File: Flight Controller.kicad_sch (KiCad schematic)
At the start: 92 parts, among them IC1 ICM-20689, IC2 AT7456E, J1 Micro_SD_Card, P1 USB_C_Plug_USB2.0, Q1 BC817W, SW2 SW_SPDT_321, U1 NCP1117-3.3_SOT223, U1 STM32F405RGTx, U2 LM2575-5.0BU, U3 BMP280, Y1 Resonator

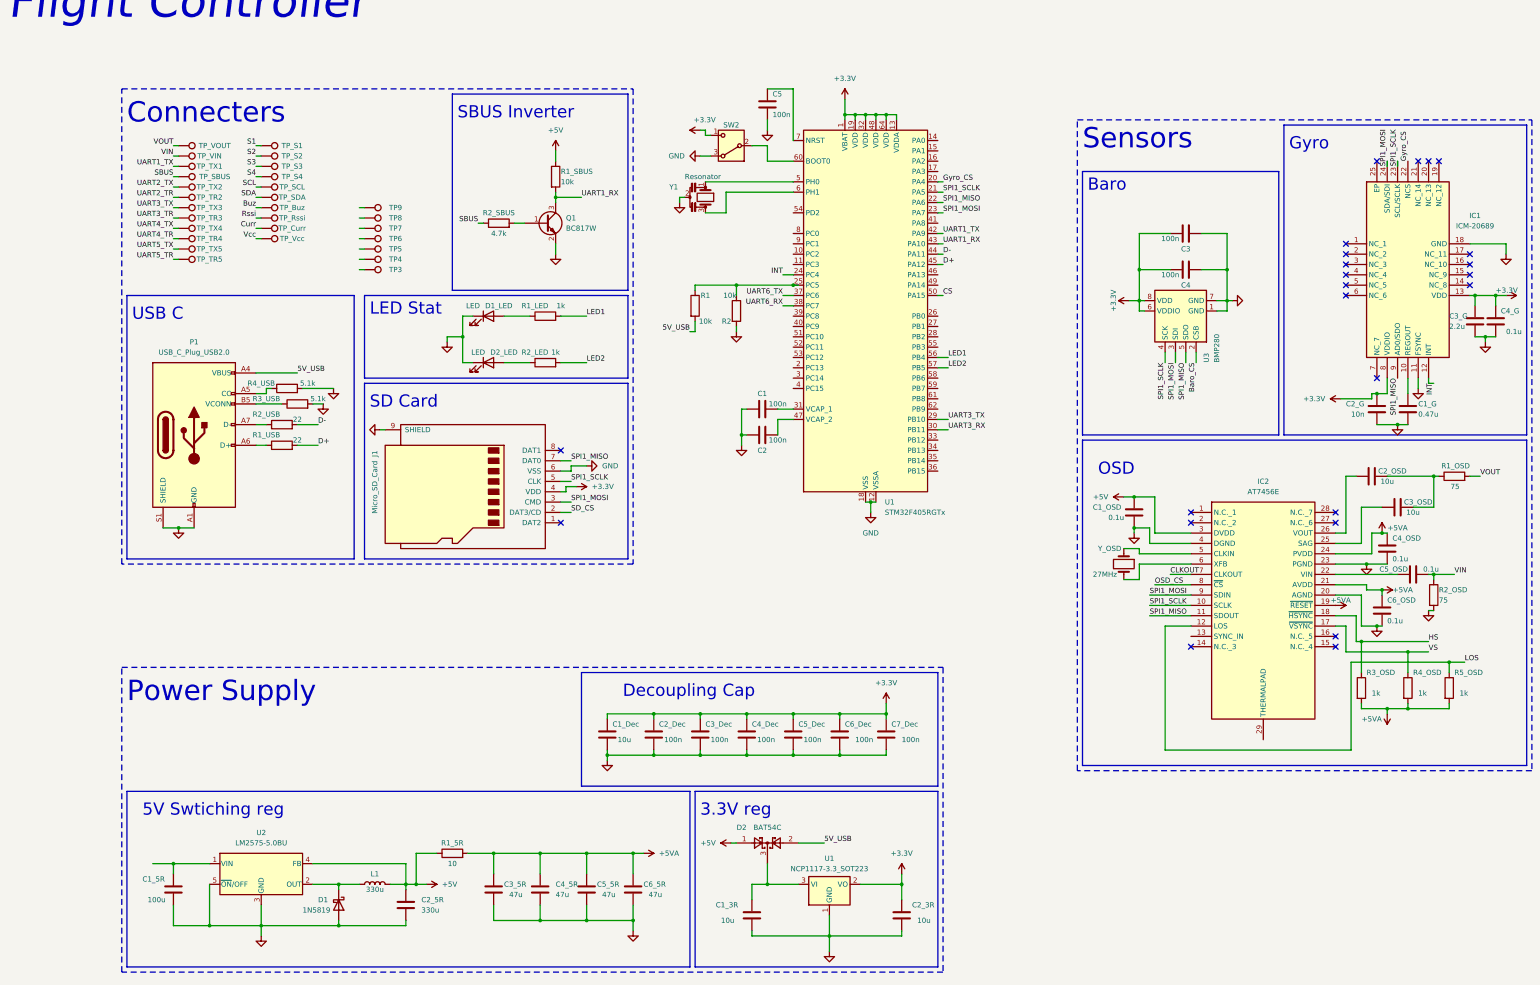
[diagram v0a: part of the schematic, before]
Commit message: schematic update
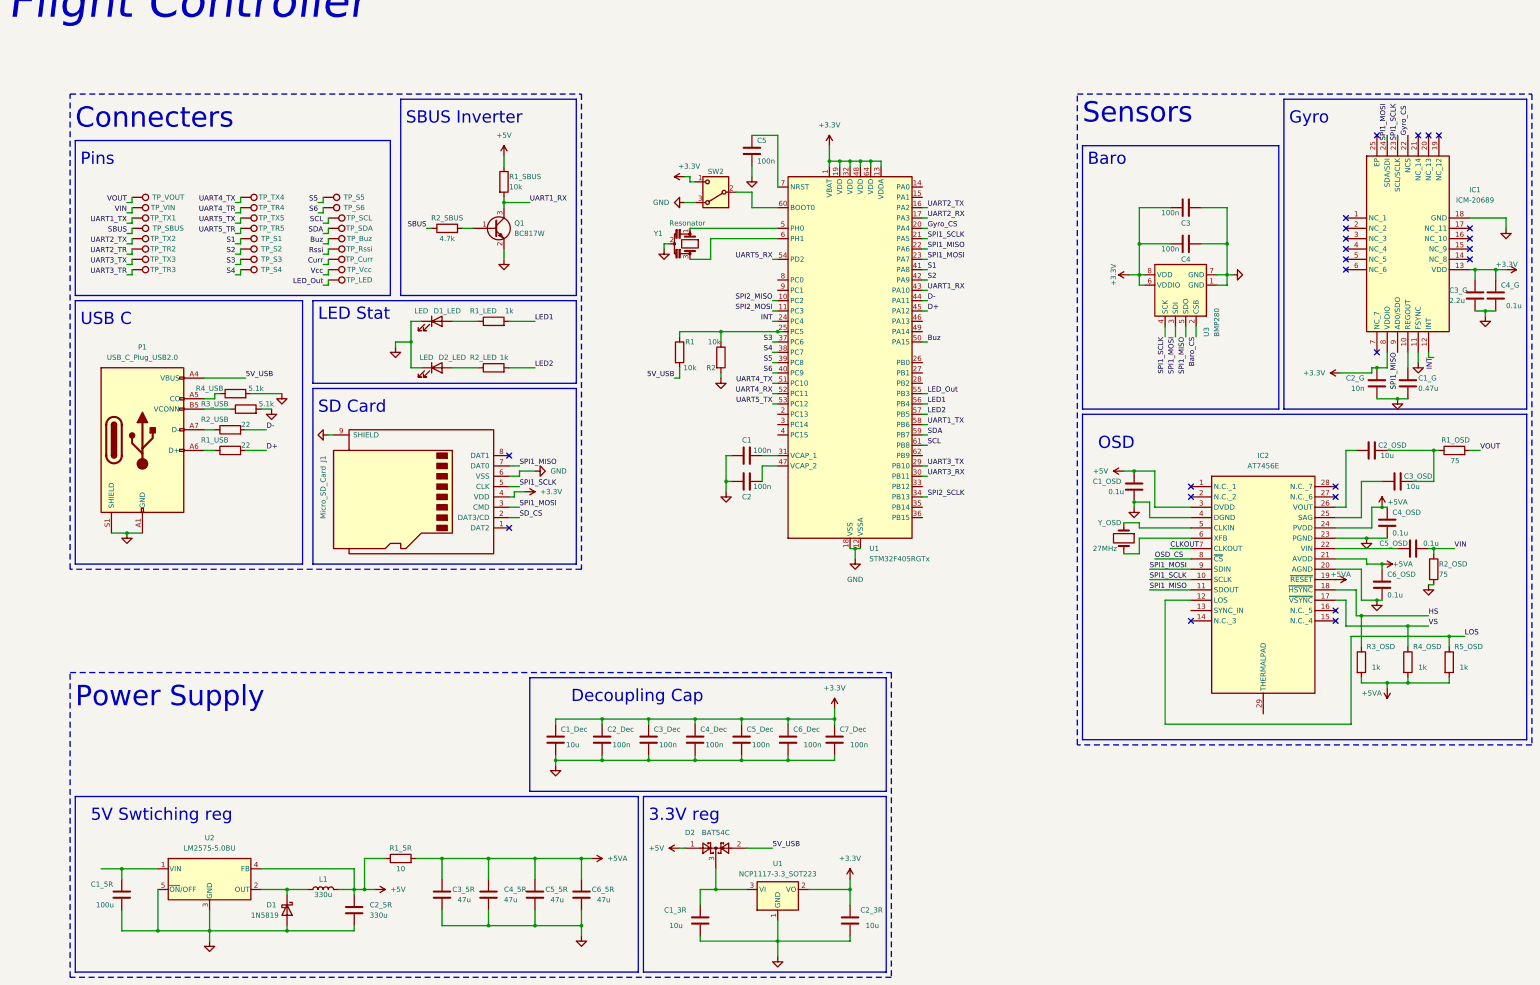
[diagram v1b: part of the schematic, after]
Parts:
- removed TP3, TP4, TP6, TP7: TestPoint, TestPoint:TestPoint_Pad_D2.5mm, symbol Connector:TestPoint
- renumbered TP5 to TP_LED, TP9 to TP_S5, TP8 to TP_S6
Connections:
- net CS is gone; now on net Buz: U1.50 (PA15)
- net UART6_RX is gone; now on net S4: U1.38 (PC7)
- net UART6_TX is gone; now on net S3: U1.37 (PC6)
- net S1: now also U1.41 (PA8)
- net S2: now also U1.42 (PA9)
- net SCL: now also U1.61 (PB8)
- net SDA: now also U1.59 (PB7)
- net UART1_TX: now also U1.58 (PB6); no longer U1.42 (PA9)
- net UART2_TX: now also U1.16 (PA2)
- net UART4_TX: now also U1.51 (PC10)
- net UART5_TX: now also U1.53 (PC12)
- net LED_Out: now reaches TP_LED.1
- net LED_Out: now also U1.55 (PB3)
- net S6: now reaches TP_S6.1
- net S6: now also U1.40 (PC9)
- net SPI2_MISO: now reaches U1.10 (PC2)
- net SPI2_MOSI: now reaches U1.11 (PC3)
- net UART2_RX: now reaches U1.17 (PA3)
- net SPI2_SCLK: now reaches U1.34 (PB13)
- net S5: now reaches U1.39 (PC8)
- net S5: now also TP_S5.1
- net UART4_RX: now reaches U1.52 (PC11)
- net UART5_RX: now reaches U1.54 (PD2)
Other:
- note added: "Pins"
- moved on the sheet: C1, C1_3R, C1_5R, C1_Dec, C1_G, C1_OSD, C2, C2_3R, C2_5R, C2_Dec, C2_G, C2_OSD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

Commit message: Update Schematic
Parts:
- removed C3_5R, C4_5R, C5_5R, C6_5R: 47u, symbol Device:C
- removed R1_5R: 10, symbol Device:R
- added H1, H2, H3, H4: MountingHole_Pad, symbol Mechanical:MountingHole_Pad
- added R3_I2C1, R3_I2C2: 5.1k, symbol Device:R
- added SW1: SW_Push, symbol Switch:SW_Push
- added TP_3V1, TP_3V2, TP_5V1, TP_5V10, TP_5V11, TP_5V12, TP_5V2, TP_5V3, TP_5V4, TP_5V5, TP_5V6, TP_5V7, TP_5V8, TP_5V9, TP_GND1, TP_GND10, TP_GND11, TP_GND12, TP_GND13, TP_GND14, TP_GND2, TP_GND3, TP_GND4, TP_GND5, TP_GND6, TP_GND7, TP_GND8, TP_GND9: TestPoint, TestPoint:TestPoint_Pad_D2.5mm, symbol Connector:TestPoint
- renumbered TP_VIN to TP_CAM, TP_TR2 to TP_RX2, TP_TR3 to TP_RX3, TP_TR4 to TP_RX4, TP_TR5 to TP_RX5, TP_Vcc to TP_VBAT, TP_VOUT to TP_VTX
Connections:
- net UART2_TR is gone; now on net UART2_RX: TP_RX2.1
- net UART3_TR is gone; now on net UART3_RX: TP_RX3.1
- net UART4_TR is gone; now on net UART4_RX: TP_RX4.1
- net UART5_TR is gone; now on net UART5_RX: TP_RX5.1
- net +3.3V: now also R3_I2C1.1, R3_I2C2.2, TP_3V1.1, TP_3V2.1
- net +5V: now also TP_5V1.1, TP_5V10.1, TP_5V11.1, TP_5V12.1, TP_5V2.1, TP_5V3.1, TP_5V4.1, TP_5V5.1, TP_5V6.1, TP_5V7.1, TP_5V8.1, TP_5V9.1
- net Curr: now also U1.14 (PA0)
- net GND: now also H1.1, H2.1, H3.1, H4.1, SW1.2, TP_GND1.1, TP_GND10.1, TP_GND11.1, TP_GND12.1, TP_GND13.1, TP_GND14.1, TP_GND2.1, TP_GND3.1, TP_GND4.1, TP_GND5.1, TP_GND6.1, TP_GND7.1, TP_GND8.1, TP_GND9.1
- net Gyro_CS: no longer U1.20 (PA4)
- net Rssi: now also U1.15 (PA1)
- net SBUS: now also TP_TX1.1; no longer TP_SBUS.1
- net SPI1_MISO: no longer IC2.11 (SDOUT)
- net SPI1_MOSI: no longer IC2.9 (SDIN)
- net SPI1_SCLK: no longer IC2.10 (SCLK)
- net SPI2_MISO: now also IC2.11 (SDOUT)
- net SPI2_MOSI: now also IC2.9 (SDIN)
- net SPI2_SCLK: now also IC2.10 (SCLK)
- net UART1_RX: now also TP_SBUS.1; no longer Q1.3 (C), R1_SBUS.2
- net UART1_TX: now also Q1.3 (C), R1_SBUS.2; no longer TP_TX1.1
- net at C5.1, U1.7 (NRST): now also SW1.1
- net SCL renamed I2C_SCL
- net I2C_SCL: now also R3_I2C2.1
- net SDA renamed I2C_SDA
- net I2C_SDA: now also R3_I2C1.2
- net Vcc renamed VBAT
- net VBAT: now also U1.20 (PA4)
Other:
- note added: "Buzzer"
- note added: "Camera"
- note added: "Currents"
- note added: "I2C"
- note added: "LED"
- note added: "Mounting Holes"
- note added: "Power"
- note added: "Signal"
- note added: "UARTS"
- note added: "VTX"
- note removed: "Pins"
- moved on the sheet: C1, C1_3R, C1_5R, C1_Dec, C1_G, C1_OSD, C2, C2_3R, C2_5R, C2_Dec, C2_G, C2_OSD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

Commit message: Update Schematic
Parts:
- added TP_VBAT+, TP_VBAT-: TestPoint, TestPoint:TestPoint_Pad_D2.5mm, symbol Connector:TestPoint
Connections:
- net Baro_CS: now also U1.8 (PC0)
- net GND: now also TP_VBAT-.1
- net Gyro_CS: now also U1.9 (PC1)
- net OSD_CS: now also U1.26 (PB0)
- net SD_CS: now also U1.27 (PB1)
- net SPI1_MISO: no longer J1.7 (DAT0)
- net SPI1_MOSI: no longer J1.3 (CMD)
- net SPI1_SCLK: no longer J1.5 (CLK)
- net SPI2_MISO: now also J1.7 (DAT0)
- net SPI2_MOSI: now also J1.3 (CMD)
- net SPI2_SCLK: now also J1.5 (CLK)
- net VBAT: no longer U1.20 (PA4)
- new net VBAT+: TP_VBAT+.1, U1.20 (PA4)
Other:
- note added: "Battery"
- moved on the sheet: H1, H2, H3, H4

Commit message: Updated Schematics
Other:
- note added: "FAFO Flight Controller"
- note removed: "Flight Controller"
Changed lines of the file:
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@@
     (effects (font (size 3 3)) (justify left bottom))
   )
-  (text "Flight Controller" (at 15.24 30.48 0)
+  (text "FAFO Flight Controller" (at 15.24 30.48 0)
     (effects (font (size 10 10) italic) (justify left bottom))
   )

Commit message: Finshed Schematics and started with layout
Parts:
- removed C1_5R: 100u, symbol Device:C
- removed C2_5R: 330u, symbol Device:C
- removed D1: 1N5819, Diode_THT:D_DO-41_SOD81_P10.16mm_Horizontal, symbol Diode:1N5819
- removed P1: USB_C_Plug_USB2.0, symbol Connector:USB_C_Plug_USB2.0
- removed R1_USB, R2_USB: 22, symbol Device:R
- removed R3_USB, R4_USB: 5.1k, symbol Device:R
- removed SW2: SW_SPDT_321, symbol Switch:SW_SPDT_321
- removed U2: LM2575-5.0BU, Package_TO_SOT_SMD:TO-263-5_TabPin3, symbol Regulator_Switching:LM2575-5.0BU
- added C1out_5R1, C2out_5R1: 22u, Capacitor_SMD:C_0805_2012Metric, symbol Device:C
- added Cboot_5R1, Cin3_5R1: 0.1u, Capacitor_SMD:C_0402_1005Metric, symbol Device:C
- added Cin2_5R1, Cin_5R1: 4.7u, Capacitor_SMD:C_0805_2012Metric, symbol Device:C
- added J2: USB_C_Receptacle_USB2.0_14P, Connector_USB:USB_C_Receptacle_HRO_TYPE-C-31-M-12, symbol Connector:USB_C_Receptacle_USB2.0_14P
- added JP1: SolderJumper_3_Open, Jumper:SolderJumper-3_P1.3mm_Open_Pad1.0x1.5mm_NumberLabels, symbol Jumper:SolderJumper_3_Open
- added R3_USB2, R4_USB2: 5.1k, Resistor_SMD:R_0603_1608Metric, symbol Device:R
- added Rfbb_5R1: 13.7k, Resistor_SMD:R_0805_2012Metric, symbol Device:R
- added Rfbt_5R1: 100k, Resistor_SMD:R_1206_3216Metric, symbol Device:R
- added U2: LMR51430, Package_TO_SOT_SMD:SOT-23-6, symbol Regulator_Switching:LMR51430
- 8M1: renamed from Y1; footprint Crystal:Resonator_Murata_CSTLSxxxX-3Pin_W5.5mm_H3.0mm -> Crystal:Resonator_SMD_Murata_CSTxExxV-3Pin_3.0x1.1mm
- C1, C2, C3, C4, C5: footprint (none) -> Capacitor_SMD:C_0402_1005Metric
- C1_3R1: renamed from C1_3R; footprint (none) -> Capacitor_SMD:C_0805_2012Metric
- C1_Dec1: renamed from C1_Dec; footprint (none) -> Capacitor_SMD:C_0805_2012Metric
- C1_G1: renamed from C1_G; footprint (none) -> Capacitor_SMD:C_0402_1005Metric
- C1_OSD1: renamed from C1_OSD; footprint (none) -> Capacitor_SMD:C_0402_1005Metric
- C2_3R1: renamed from C2_3R; footprint (none) -> Capacitor_SMD:C_0805_2012Metric
- C2_Dec1: renamed from C2_Dec; footprint (none) -> Capacitor_SMD:C_0402_1005Metric
- C2_G1: renamed from C2_G; footprint (none) -> Capacitor_SMD:C_0402_1005Metric
- C2_OSD1: renamed from C2_OSD; footprint (none) -> Capacitor_SMD:C_0805_2012Metric
- C3_Dec1: renamed from C3_Dec; footprint (none) -> Capacitor_SMD:C_0402_1005Metric
- C3_G1: renamed from C3_G; footprint (none) -> Capacitor_SMD:C_0805_2012Metric
- C3_OSD1: renamed from C3_OSD; footprint (none) -> Capacitor_SMD:C_0805_2012Metric
- C4_Dec1: renamed from C4_Dec; footprint (none) -> Capacitor_SMD:C_0402_1005Metric
- C4_G1: renamed from C4_G; footprint (none) -> Capacitor_SMD:C_0402_1005Metric
- C4_OSD1: renamed from C4_OSD; footprint (none) -> Capacitor_SMD:C_0402_1005Metric
- C5_Dec1: renamed from C5_Dec; footprint (none) -> Capacitor_SMD:C_0402_1005Metric
- C5_OSD1: renamed from C5_OSD; footprint (none) -> Capacitor_SMD:C_0402_1005Metric
- C6_Dec1: renamed from C6_Dec; footprint (none) -> Capacitor_SMD:C_0402_1005Metric
- C6_OSD1: renamed from C6_OSD; footprint (none) -> Capacitor_SMD:C_0402_1005Metric
- C7_Dec1: renamed from C7_Dec; footprint (none) -> Capacitor_SMD:C_0402_1005Metric
- D1_LED1: renamed from D1_LED; footprint (none) -> LED_SMD:LED_0402_1005Metric
- D2_LED1: renamed from D2_LED; footprint (none) -> LED_SMD:LED_0402_1005Metric
- H1, H2, H3, H4: footprint (none) -> MountingHole:MountingHole_3.2mm_M3_DIN965_Pad
- IC1: footprint QFN50P400X400X95-25N-D -> ICM-20689:QFN50P400X400X95-24N
- IC2: footprint SOP65P640X120-29N -> MAX7456EUI:SOP65P637X110-28N
- J1: footprint Connector_Card:microSD_HC_Molex_104031-0811 -> Connector_Card:microSD_HC_Molex_47219-2001
- L1: value 330u -> 6.8u; footprint (none) -> Inductor_SMD:L_Abracon_ASPI-0630LR
- R1, R2: footprint (none) -> Resistor_SMD:R_1206_3216Metric
- R1_LED1: renamed from R1_LED; footprint (none) -> Resistor_SMD:R_0805_2012Metric
- R1_OSD1: renamed from R1_OSD; footprint (none) -> Resistor_SMD:R_0603_1608Metric
- R1_SBUS1: renamed from R1_SBUS; footprint (none) -> Resistor_SMD:R_1206_3216Metric
- R2_LED1: renamed from R2_LED; footprint (none) -> Resistor_SMD:R_0805_2012Metric
- R2_OSD1: renamed from R2_OSD; footprint (none) -> Resistor_SMD:R_0603_1608Metric
- R2_SBUS1: renamed from R2_SBUS; footprint (none) -> Resistor_SMD:R_0805_2012Metric
- R3_I2C1, R3_I2C2: footprint (none) -> Resistor_SMD:R_0603_1608Metric
- R3_OSD1: renamed from R3_OSD; footprint (none) -> Resistor_SMD:R_0805_2012Metric
- R4_OSD1: renamed from R4_OSD; footprint (none) -> Resistor_SMD:R_0805_2012Metric
- R5_OSD1: renamed from R5_OSD; footprint (none) -> Resistor_SMD:R_0805_2012Metric
- SW_NRST1: renamed from SW1; footprint (none) -> Button_Switch_SMD:SW_Tactile_SPST_NO_Straight_CK_PTS636Sx25SMTRLFS
- TP_3V1, TP_3V2, TP_5V1, TP_5V10, TP_5V11, TP_5V12, TP_5V2, TP_5V3, TP_5V4, TP_5V5, TP_5V6, TP_5V7, TP_5V8, TP_5V9, TP_GND1, TP_GND10, TP_GND11, TP_GND12, TP_GND13, TP_GND14, TP_GND2, TP_GND3, TP_GND4, TP_GND5, TP_GND6, TP_GND7, TP_GND8, TP_GND9, TP_RX2, TP_RX3, TP_RX4, TP_RX5, TP_S1, TP_S2, TP_S3, TP_S4, TP_S5, TP_S6, TP_TX1, TP_TX2, TP_TX3, TP_TX4, TP_TX5: footprint TestPoint:TestPoint_Pad_D2.5mm -> Connector:Soldier_Pad
- TP_Buz1: renamed from TP_Buz; footprint TestPoint:TestPoint_Pad_D2.5mm -> Connector:Soldier_Pad
- TP_CAM1: renamed from TP_CAM; footprint TestPoint:TestPoint_Pad_D2.5mm -> Connector:Soldier_Pad
- TP_Curr1: renamed from TP_Curr; footprint TestPoint:TestPoint_Pad_D2.5mm -> Connector:Soldier_Pad
- TP_LED1: renamed from TP_LED; footprint TestPoint:TestPoint_Pad_D2.5mm -> Connector:Soldier_Pad
- TP_Rssi1: renamed from TP_Rssi; footprint TestPoint:TestPoint_Pad_D2.5mm -> Connector:Soldier_Pad
- TP_SBUS1: renamed from TP_SBUS; footprint TestPoint:TestPoint_Pad_D2.5mm -> Connector:Soldier_Pad
- TP_SCL1: renamed from TP_SCL; footprint TestPoint:TestPoint_Pad_D2.5mm -> Connector:Soldier_Pad
- TP_SDA1: renamed from TP_SDA; footprint TestPoint:TestPoint_Pad_D2.5mm -> Connector:Soldier_Pad
- TP_VBAT1: renamed from TP_VBAT; footprint TestPoint:TestPoint_Pad_D2.5mm -> Connector:Soldier_Pad
- TP_VTX1: renamed from TP_VTX; footprint TestPoint:TestPoint_Pad_D2.5mm -> Connector:Soldier_Pad
- Y_OSD1: renamed from Y_OSD; footprint (none) -> Oscillator:Oscillator_SMD_Abracon_ASCO-4Pin_1.6x1.2mm
- renumbered TP_VBAT+ to TP_VBAT+1, TP_VBAT- to TP_VBAT-1, U1 to U4
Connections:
- net +5VA is gone; now on net +5V: C4_OSD1.1, C6_OSD1.1, IC2.19 (~{RESET}), IC2.21 (AVDD), IC2.24 (PVDD), R3_OSD1.2, R4_OSD1.2, R5_OSD1.2
- net VBAT is gone; now on net VBAT+: TP_VBAT1.1
- net +3.3V: now also JP1.3 (B)
- net +5V: now also C1out_5R1.1, C2out_5R1.1, Rfbt_5R1.1
- net 5V_USB: now also J2.A4 (VBUS), J2.A9 (VBUS), J2.B4 (VBUS), J2.B9 (VBUS)
- net D+: now also J2.A6 (D+), J2.B6 (D+)
- net D-: now also J2.A7 (D-), J2.B7 (D-)
- net GND: now also IC2.29 (THERMALPAD), J2.A1 (GND), J2.A12 (GND), J2.B1 (GND), J2.B12 (GND), J2.S1 (SHIELD), JP1.1 (A), R3_USB2.2, R4_USB2.2
- net VBAT+: now also Cin2_5R1.1, Cin3_5R1.2, Cin_5R1.1, U2.3 (VIN), U2.5 (EN)
- net at U1.60 (BOOT0): now also JP1.2 (C)
- net at L1.1: now also Cboot_5R1.2, U2.2 (SW)
- new net: C1out_5R1.2, C2out_5R1.2, Cin2_5R1.2, Cin3_5R1.1, Cin_5R1.2, Rfbb_5R1.2, U2.1 (GND)
- new net: Rfbb_5R1.1, Rfbt_5R1.2, U2.4 (FB)
- new net: Cboot_5R1.1, U2.6 (CB)
- new net: J2.A5 (CC1), R4_USB2.1
- new net: J2.B5 (CC2), R3_USB2.1
- no-connect marks 24 -> 36
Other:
- moved on the sheet: C1_3R1, C5, SW_NRST1

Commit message: Power Supply Sch Udpate
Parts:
- added C1out_5R2, C2out_5R2: 22u, Capacitor_SMD:C_0805_2012Metric, symbol Device:C
- added Cboot_5R2, Cin3_5R2: 0.1u, Capacitor_SMD:C_0402_1005Metric, symbol Device:C
- added Cin2_5R2, Cin_5R2: 4.7u, Capacitor_SMD:C_0805_2012Metric, symbol Device:C
- added L2: 6.8u, Inductor_SMD:L_Abracon_ASPI-0630LR, symbol Device:L
- added Rfbb_5R2: 6.2k, Resistor_SMD:R_0805_2012Metric, symbol Device:R
- added Rfbt_5R2: 100k, Resistor_SMD:R_1206_3216Metric, symbol Device:R
- added U5: LMR51430, Package_TO_SOT_SMD:SOT-23-6, symbol Regulator_Switching:LMR51430
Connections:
- net +5V: now also C1out_5R2.1, C2out_5R2.1, L2.2, Rfbt_5R2.1
- net VBAT+: now also Cin2_5R2.1, Cin3_5R2.2, Cin_5R2.1, U5.3 (VIN), U5.5 (EN)
- new net: C1out_5R2.2, C2out_5R2.2, Cin2_5R2.2, Cin3_5R2.1, Cin_5R2.2, Rfbb_5R2.2, U5.1 (GND)
- new net: Cboot_5R2.1, U5.6 (CB)
- new net: Cboot_5R2.2, L2.1, U5.2 (SW)
- new net: Rfbb_5R2.1, Rfbt_5R2.2, U5.4 (FB)
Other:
- note added: "10V Swtiching reg"
- moved on the sheet: 8M1, C1, C1_3R1, C1_Dec1, C1out_5R1, C2, C2_3R1, C2_Dec1, C2out_5R1, C3_Dec1, C4_Dec1, C5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
